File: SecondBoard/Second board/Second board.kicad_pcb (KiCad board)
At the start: 2 copper layers, 5 parts

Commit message: SecondBoard Rond m130
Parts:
- added J1: Conn_01x04_Socket, TerminalBlock_Phoenix:TerminalBlock_Phoenix_MKDS-1,5-4_1x04_P5.00mm_Horizontal, F.Cu at (93.7, 93.2)
- added J2: Conn_01x04_Socket, TerminalBlock_Phoenix:TerminalBlock_Phoenix_MKDS-1,5-4_1x04_P5.00mm_Horizontal, F.Cu at (93.8, 70.3)
- GYBME1: footprint custom footprints:GY-BME280_P -> custom footprints:Sans titre
- moved SecondBoardConnector1 56.4 mm to (200.8, 96.8)
- moved LightSensor1 45.4 mm to (149.2, 126.8), turned to 180 degrees
- moved SPS30 45.0 mm to (158.0, 44.9), turned to 180 degrees
- moved ZX-MPU1 31.7 mm to (139.5, 106.6), turned to 90 degrees
- moved GYBME1 17.3 mm to (177.0, 133.9)
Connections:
- GYBME1 pad 3: Net-(GYBME1-SCL) -> unconnected-(GYBME1-GND-Pad3)
- GYBME1 pad 4: Net-(GYBME1-SDA) -> Net-(GYBME1-SCK)
- GYBME1 pad 6: unconnected-(GYBME1-SDO-Pad6) -> Net-(GYBME1-SDI)
- LightSensor1 pad 4: Net-(GYBME1-SCL) -> Net-(GYBME1-SCK)
- LightSensor1 pad 5: Net-(GYBME1-SDA) -> Net-(GYBME1-SDI)
- SPS30 pad 2: Net-(GYBME1-SDA) -> Net-(GYBME1-SDI)
- SPS30 pad 3: Net-(GYBME1-SCL) -> Net-(GYBME1-SCK)
- SecondBoardConnector1 pad 10: Net-(GYBME1-SDA) -> Net-(GYBME1-SDI)
- SecondBoardConnector1 pad 8: Net-(GYBME1-SCL) -> Net-(GYBME1-SCK)
- ZX-MPU1 pad 3: Net-(GYBME1-SCL) -> Net-(GYBME1-SCK)
- ZX-MPU1 pad 4: Net-(GYBME1-SDA) -> Net-(GYBME1-SDI)
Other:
- board outline added: 130 x 130 mm

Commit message: Plan de masse Update
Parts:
- added U1: ESP32-CAM, ESP32-CAM:ESP32-CAM, F.Cu at (147.3, 70.1)
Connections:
- SecondBoardConnector1 pad 3: unconnected-(SecondBoardConnector1-Pad3) -> Net-(SecondBoardConnector1-Pad3)
- SecondBoardConnector1 pad 5: unconnected-(SecondBoardConnector1-Pad5) -> Net-(SecondBoardConnector1-Pad5)
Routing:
- net Net-(GYBME1-SDI): track 0.00 -> 380.7 mm
- net +5V: track 0.00 -> 259.8 mm
- net Net-(GYBME1-SCK): track 0.00 -> 230.6 mm
- net +3.3V: track 0.00 -> 145.3 mm
- net Net-(SecondBoardConnector1-Pad3): track 0.00 -> 90.8 mm
- net Net-(SecondBoardConnector1-Pad5): track 0.00 -> 81.7 mm
- added copper zone on B.Cu, net GND

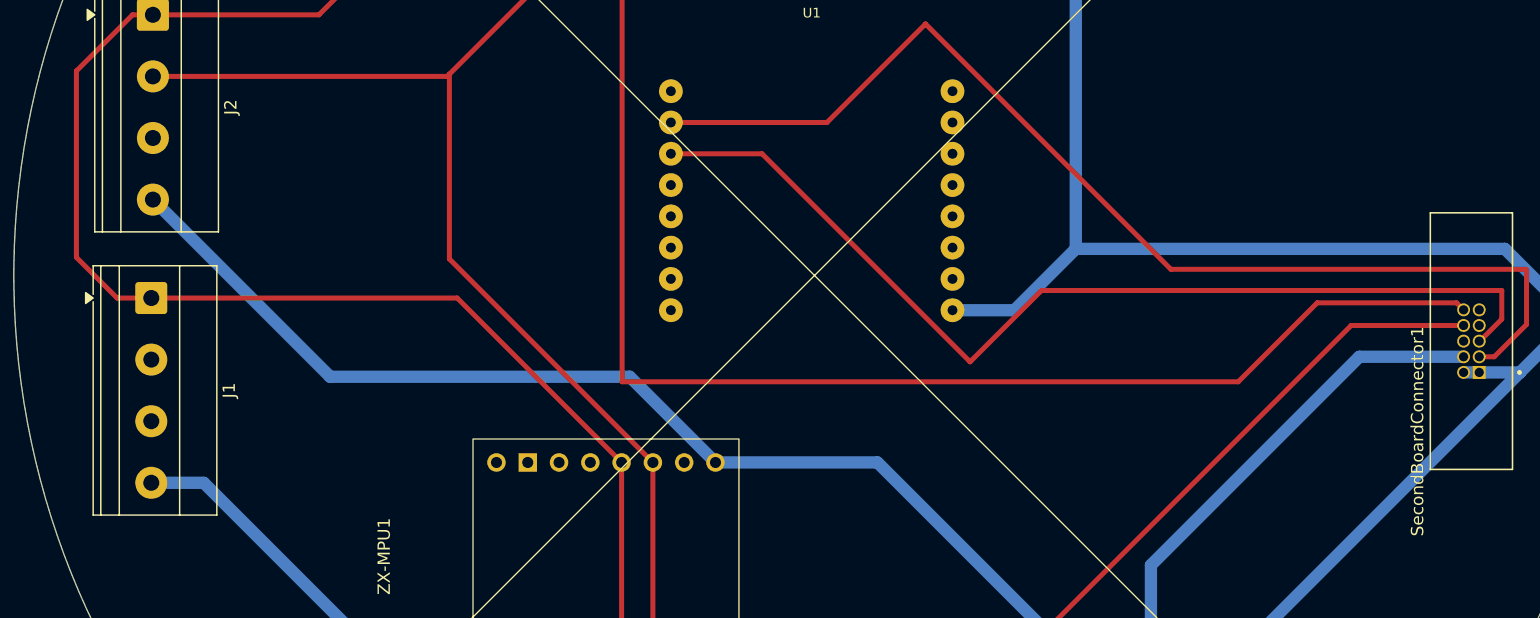
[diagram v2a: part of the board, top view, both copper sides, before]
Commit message: rajout gnd
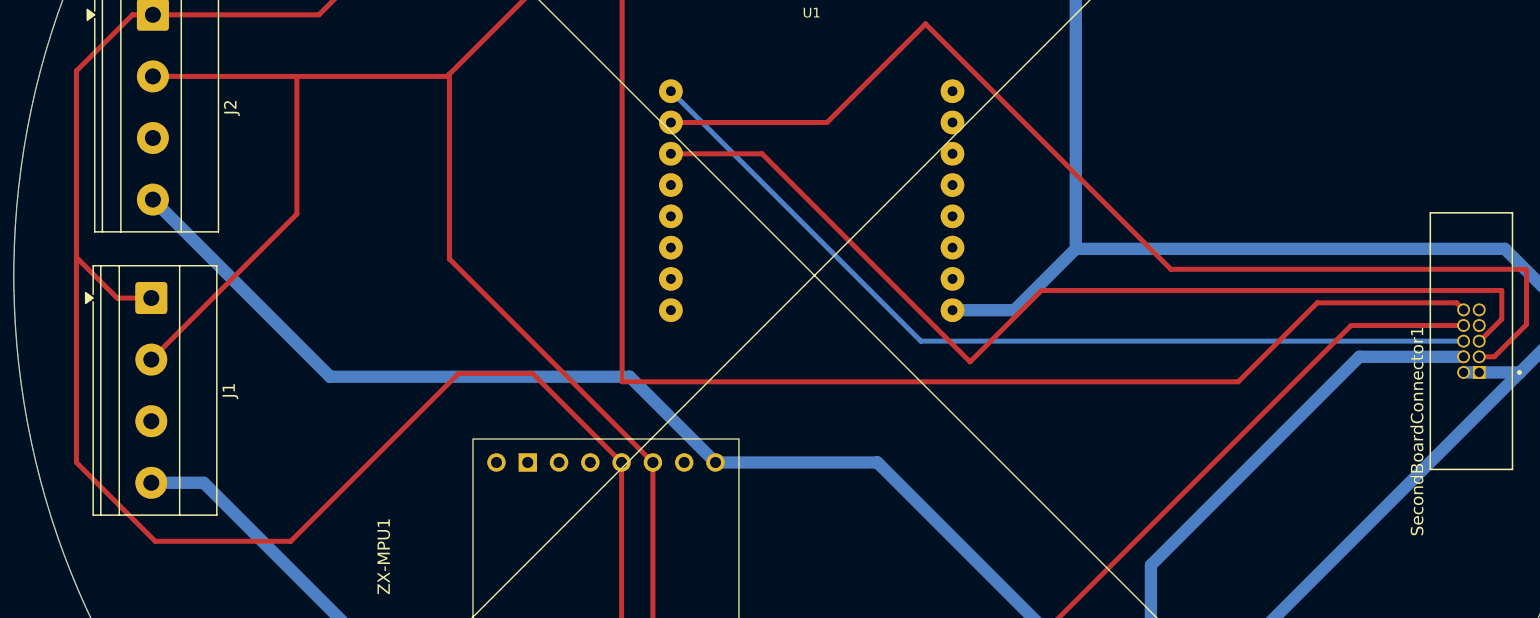
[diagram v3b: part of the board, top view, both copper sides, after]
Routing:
- net GND: track 0.00 -> 72.8 mm
- net Net-(GYBME1-SDI): track 380.7 -> 409.2 mm
- net Net-(GYBME1-SCK): track 230.6 -> 258.5 mm
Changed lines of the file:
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@@
+	)
+	(segment
+		(start 200.21 96.75)
+		(end 156.15 96.75)
+		(width 0.4064)
+		(layer "B.Cu")
+		(net 6)
+	)
+	(segment
+		(start 156.15 96.75)
+		(end 135.86 76.46)
+		(width 0.4064)
+		(layer "B.Cu")
+		(net 6)
 	)
 	(segment
@@
 	)
 	(segment
+		(start 93.68 98.25)
+		(end 105.5 86.43)
+		(width 0.4064)
+		(layer "F.Cu")
+		(net 15)
+	)
+	(segment
 		(start 155.75 131.16)
 		(end 155.75 130.811139)
@@
 	)
 	(segment
+		(start 105.5 75.26)
+		(end 117.6975 75.26)
+		(width 0.4064)
+		(layer "F.Cu")
+		(net 15)
+	)
+	(segment
 		(start 155.75 130.811139)
 		(end 191.081139 95.48)
@@
 	)
 	(segment
+		(start 105.5 86.43)
+		(end 105.5 75.26)
+		(width 0.4064)
+		(layer "F.Cu")
+		(net 15)
+	)
+	(segment
 		(start 155.092128 131.817872)
 		(end 155.75 131.16)
@@
 	(segment
 		(start 93.81 75.26)
-		(end 117.6975 75.26)
+		(end 105.5 75.26)
 		(width 0.4064)
 		(layer "F.Cu")
@@
 	)
 	(segment
-		(start 118.51 93.25)
-		(end 93.68 93.25)
+		(start 87.6 89.95)
+		(end 87.6 106.6)
 		(width 0.4064)
 		(layer "F.Cu")
@@
 	)
 	(segment
+		(start 87.6 106.6)
+		(end 94 113)
+		(width 0.4064)
+		(layer "F.Cu")
+		(net 17)
+	)
+	(segment
+		(start 105 113)
+		(end 118.51 99.49)
+		(width 0.4064)
+		(layer "F.Cu")
+		(net 17)
+	)
+	(segment
 		(start 153.01 44.9475)
 		(end 131.9 66.0575)
@@
 	)
 	(segment
+		(start 118.63 99.37)
+		(end 124.63 99.37)
+		(width 0.4064)
+		(layer "F.Cu")
+		(net 17)
+	)
+	(segment
 		(start 146.6825 38.62)
 		(end 153.01 44.9475)
@@
 	)
 	(segment
+		(start 94 113)
+		(end 105 113)
+		(width 0.4064)
+		(layer "F.Cu")
+		(net 17)
+	)
+	(segment
 		(start 131.9 100.05)
 		(end 181.92 100.05)
@@
 	)
 	(segment
-		(start 131.86 106.6)
-		(end 118.51 93.25)
+		(start 118.51 99.49)
+		(end 118.63 99.37)
 		(width 0.4064)
 		(layer "F.Cu")
@@
 		(width 0.4064)
 		(layer "F.Cu")
+		(net 17)
+	)
+	(segment
+		(start 131.86 106.6)
+		(end 124.63 99.37)
+		(width 0.4064)
+		(layer "F.Cu")

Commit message: changement connecteur
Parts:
- removed SecondBoardConnector1: SecondBoard Connector, M50-3550542:HARWIN_M50-3550542
- added J3: Conn_01x10_Socket, Connector_PinSocket_2.54mm:PinSocket_1x10_P2.54mm_Vertical, B.Cu at (55.0, -11.4)
- moved GYBME1 173.1 mm to (29.8, 42.7)
- moved J1 173.1 mm to (-53.5, 2.00)
- moved J2 173.1 mm to (-53.3, -21.0)
- moved LightSensor1 173.1 mm to (2.07, 35.5)
- moved U1 173.1 mm to (0.14, -21.1)
- moved SPS30 173.1 mm to (10.9, -46.3)
- moved ZX-MPU1 173.1 mm to (-7.67, 15.3)
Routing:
- net GND: track 72.8 -> 0.00 mm
- net Net-(J3-Pin_8): track 81.7 -> 107.3 mm
- net +5V: track 259.8 -> 273.3 mm
- net +3.3V: track 145.3 -> 157.6 mm
- net Net-(GYBME1-SCK): track 258.5 -> 264.6 mm
- net Net-(GYBME1-SDI): track 409.2 -> 412.4 mm
- net Net-(J3-Pin_7): track 90.8 -> 91.9 mm
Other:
- outline, holes or cut-outs redrawn

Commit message: finished version
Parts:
- I2C-1: renamed from J1; footprint TerminalBlock_Phoenix:TerminalBlock_Phoenix_MKDS-1,5-4_1x04_P5.00mm_Horizontal -> Connector_JST:JST_XH_B4B-XH-AM_1x04_P2.50mm_Vertical
- I2C-2: renamed from J2; footprint TerminalBlock_Phoenix:TerminalBlock_Phoenix_MKDS-1,5-4_1x04_P5.00mm_Horizontal -> Connector_JST:JST_XH_B4B-XH-AM_1x04_P2.50mm_Vertical
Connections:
- J3 pad 1: +5V -> unconnected-(J3-Pin_1-Pad1)
- J3 pad 10: unconnected-(J3-Pin_10-Pad10) -> +5V
- J3 pad 2: +5V -> unconnected-(J3-Pin_2-Pad2)
- J3 pad 3: +3.3V -> Net-(J3-Pin_3)
- J3 pad 4: GND -> Net-(J3-Pin_4)
- J3 pad 5: Net-(GYBME1-SDI) -> Net-(GYBME1-SCK)
- J3 pad 6: Net-(GYBME1-SCK) -> Net-(GYBME1-SDI)
- J3 pad 7: Net-(J3-Pin_7) -> GND
- J3 pad 8: Net-(J3-Pin_8) -> +3.3V
- J3 pad 9: unconnected-(J3-Pin_9-Pad9) -> +5V
- U1 pad U0R: Net-(J3-Pin_8) -> Net-(J3-Pin_4)
- U1 pad U0T: Net-(J3-Pin_7) -> Net-(J3-Pin_3)
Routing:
- net Net-(J3-Pin_8): track 107.3 -> 0.00 mm
- net Net-(J3-Pin_4): track 0.00 -> 95.6 mm
- net Net-(J3-Pin_7): track 91.9 -> 0.00 mm
- net Net-(J3-Pin_3): track 0.00 -> 72.9 mm
- net +5V: track 273.3 -> 300.3 mm
- net Net-(GYBME1-SCK): track 264.6 -> 280.2 mm
- net Net-(GYBME1-SDI): track 412.4 -> 411.4 mm
- net +3.3V: track 157.6 -> 156.6 mm
